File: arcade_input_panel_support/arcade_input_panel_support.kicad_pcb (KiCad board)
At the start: 2 copper layers, 116.3 x 103.8 mm, 14 parts, among them J1 Conn_01x15, J10 Conn_01x02, J11 Conn_01x02, J12 Conn_01x02, J13 Conn_01x02, J14 Conn_01x02, J2 Conn_01x14, J3 Conn_01x15, J4 Conn_01x15, J5 Conn_01x05, J6 Conn_01x02, J7 Conn_01x02, J8 Conn_01x02, J9 Conn_01x02

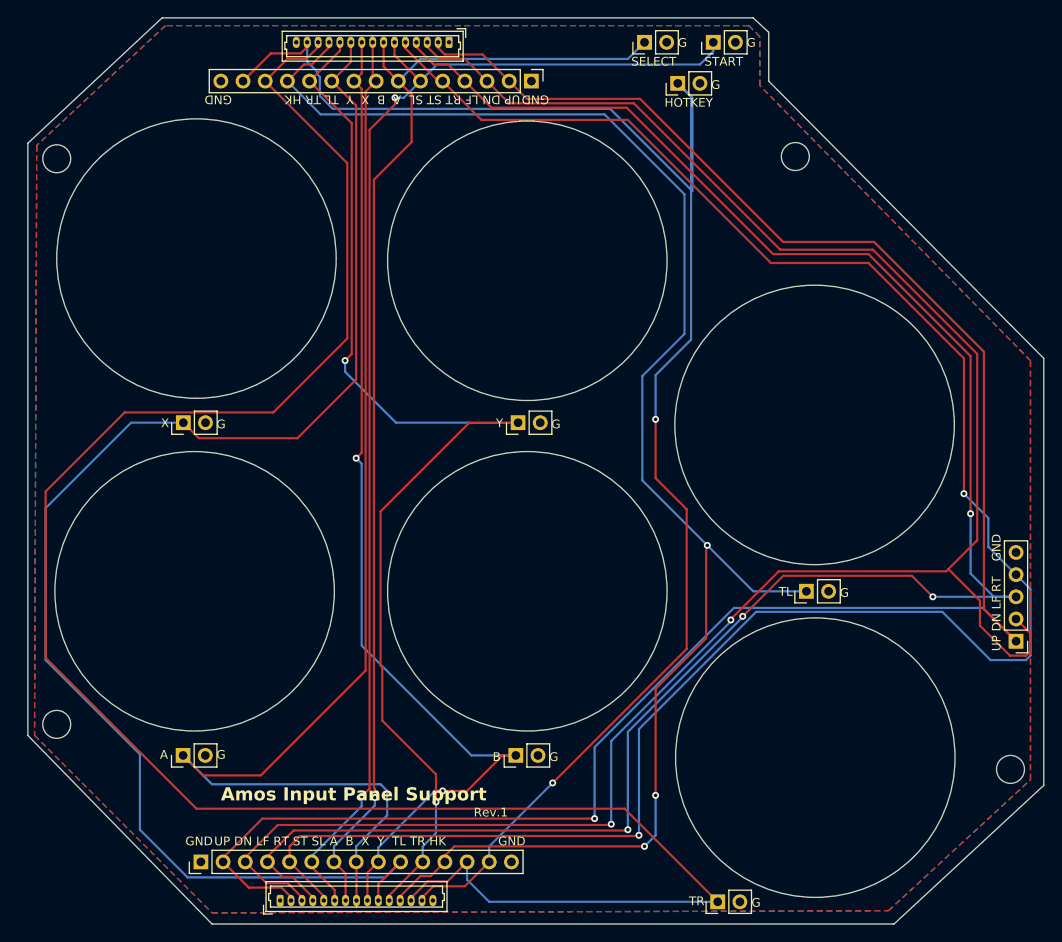
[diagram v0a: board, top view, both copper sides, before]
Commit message: 배선 최적화 및 레이아웃 변경
Signed-off-by: Ju, Gyeong-min <jcmh74@gmail.com>
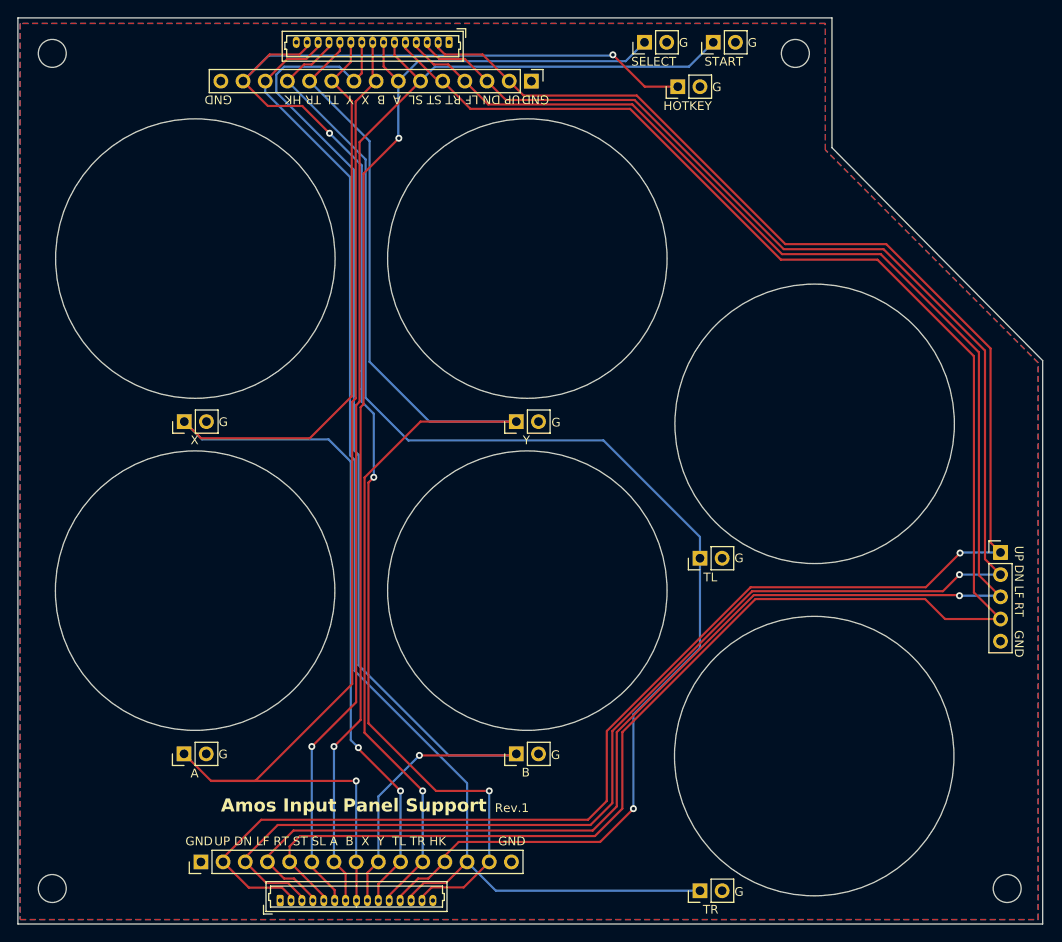
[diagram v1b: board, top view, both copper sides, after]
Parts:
- moved J12 12.8 mm to (114.0, 92.0)
- moved J5 10.3 mm to (148.5, 91.3), turned to 0 degrees
- moved J13 2.40 mm to (114.0, 130.0)
- moved J14 0.38 mm to (111.5, 38.0)
- moved J11 0.24 mm to (93.0, 76.3)
- moved J8 0.21 mm to (55.0, 114.4)
- moved J9 0.19 mm to (93.0, 114.4)
- moved J10 0.17 mm to (55.0, 76.3)
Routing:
- net /TR: track 231.3 -> 144.0 mm
- net /TL: track 185.7 -> 158.2 mm, vias 3 -> 1
- net /X: track 163.4 -> 139.0 mm, vias 0 -> 2
- net /B: track 119.9 -> 138.8 mm, vias 2 -> 1
- net /DOWN: track 232.8 -> 219.0 mm, vias 2 -> 1
- net /RIGHT: track 230.3 -> 219.2 mm, vias 2 -> 0
- net /UP: track 231.7 -> 220.7 mm
- net /HOTKEY: track 188.7 -> 179.7 mm, vias 2 -> 4
- net /A: track 138.5 -> 130.2 mm, vias 0 -> 1
- net /LEFT: track 224.5 -> 217.9 mm, vias 4 -> 1
- net /SELECT: track 134.3 -> 133.0 mm, vias 1 -> 2
- net /START: track 142.3 -> 141.1 mm, vias 2 -> 1
- net /Y: track 133.1 -> 133.4 mm, vias 2 -> 1
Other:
- board size 116.3 x 103.8 mm -> 117.3 x 103.8 mm

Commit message: 커넥터 추가
Signed-off-by: Ju, Gyeong-min <jcmh74@gmail.com>
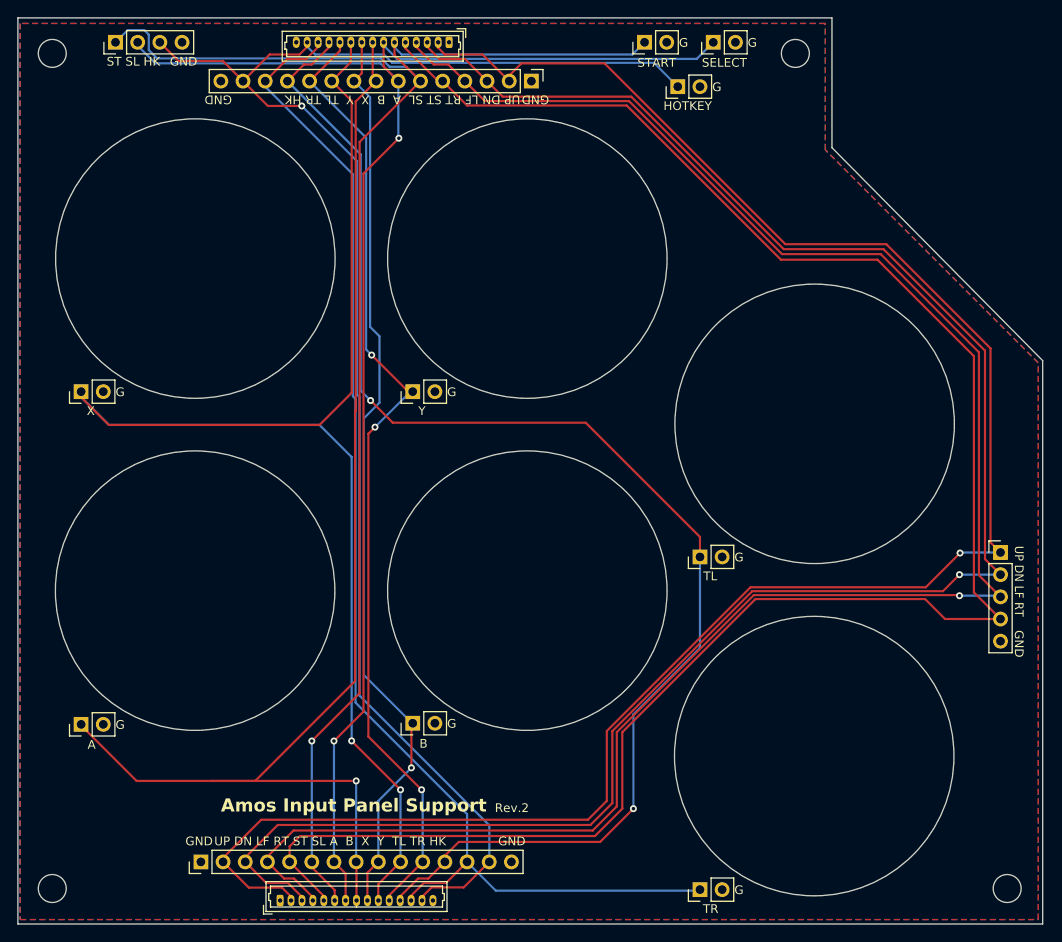
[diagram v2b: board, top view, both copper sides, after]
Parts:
- added J15: Conn_01x04, Connector_PinHeader_2.54mm:PinHeader_1x04_P2.54mm_Vertical, F.Cu at (47.1, 32.9)
- moved J9 12.4 mm to (81.2, 110.9)
- moved J11 12.3 mm to (81.2, 72.9)
- moved J10 12.3 mm to (43.2, 72.9)
- moved J8 12.3 mm to (43.2, 111.0)
- moved J6 7.87 mm to (107.7, 32.9)
- moved J7 7.87 mm to (115.6, 32.9)
- moved J12 0.15 mm to (114.0, 91.8)
- moved J13 0.13 mm to (114.0, 129.9)
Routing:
- net /SELECT: track 133.0 -> 174.1 mm
- net /START: track 141.1 -> 174.8 mm
- net /B: track 138.8 -> 105.1 mm
- net /X: track 139.0 -> 165.1 mm
- net /Y: track 133.4 -> 111.3 mm, vias 1 -> 3
- net /A: track 130.2 -> 143.5 mm
- net /UP: track 220.7 -> 222.7 mm
- net /HOTKEY: track 179.7 -> 179.2 mm, vias 4 -> 1
- net /TL: track 158.2 -> 158.1 mm, vias 1 -> 2
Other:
- board text added: "Rev.2"
- board text added: "ST SL HK"
- board text removed: "Rev.1"

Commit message: 입력 패널 버튼 서포터 rev 2
Signed-off-by: Ju, Gyeong-min <jcmh74@gmail.com>
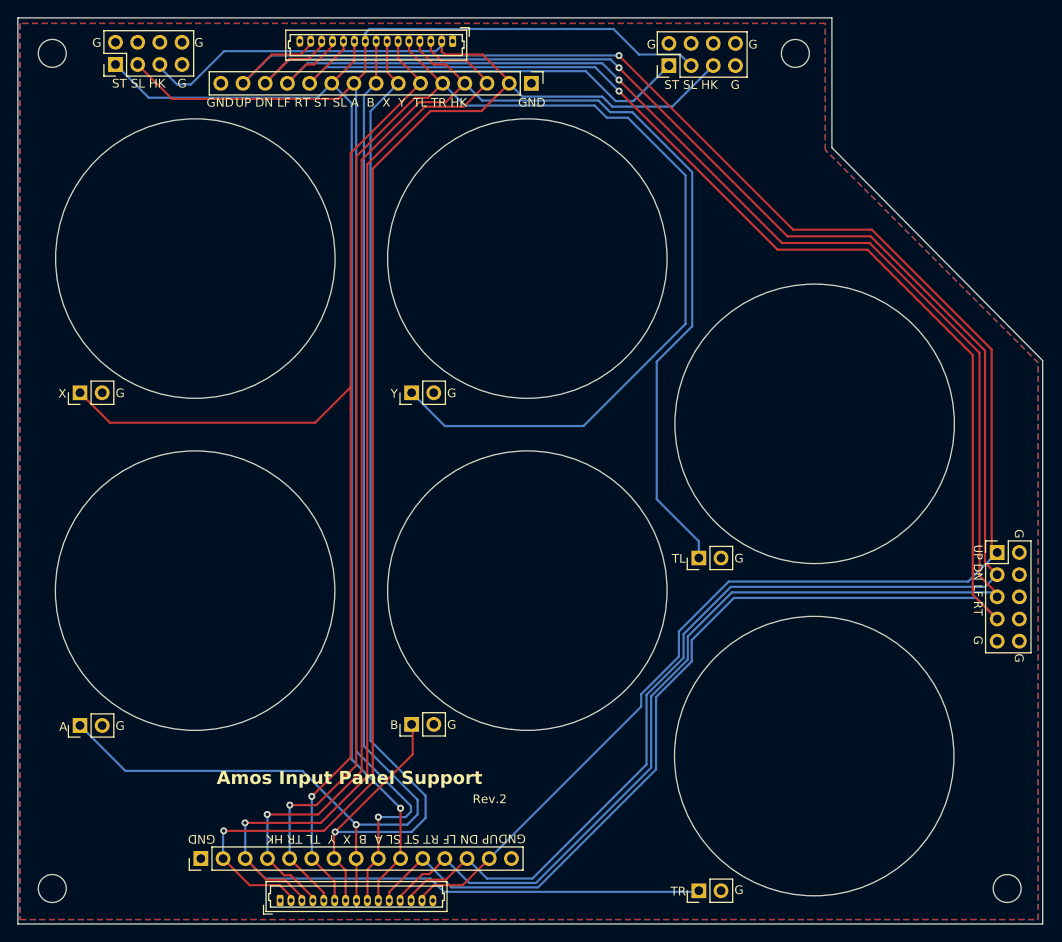
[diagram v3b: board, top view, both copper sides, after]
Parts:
- removed the J14 at (111.5, 38.0)
- removed J6: Conn_01x02, Connector_PinHeader_2.54mm:PinHeader_1x02_P2.54mm_Vertical
- removed the J7 at (115.6, 32.9)
- added J15: Conn_02x04, Connector_PinHeader_2.54mm:PinHeader_2x04_P2.54mm_Vertical, F.Cu at (110.5, 35.6)
- J14: renamed from J15; value Conn_01x04 -> Conn_02x04; footprint Connector_PinHeader_2.54mm:PinHeader_1x04_P2.54mm_Vertical -> Connector_PinHeader_2.54mm:PinHeader_2x04_P2.54mm_Vertical
- J7: renamed from J5; value Conn_01x05 -> Conn_02x05; footprint Connector_PinHeader_2.54mm:PinHeader_1x05_P2.54mm_Vertical -> Connector_PinHeader_2.54mm:PinHeader_2x05_P2.54mm_Vertical
- moved J14 2.54 mm to (47.1, 35.4)
- moved J1 0.43 mm to (85.7, 32.8)
- moved J4 0.38 mm to (56.9, 126.4)
- moved J7 0.38 mm to (148.1, 91.3)
- moved J3 0.25 mm to (94.7, 37.6)
- moved J11 0.18 mm to (81.0, 73.0)
- moved J13 0.18 mm to (113.9, 130.0)
- moved J9 0.18 mm to (81.0, 111.0)
- moved J10 0.18 mm to (43.1, 73.0)
- moved J12 0.18 mm to (113.9, 91.9)
- moved J8 0.18 mm to (43.1, 111.1)
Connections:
- J1 pad 10: /X -> /START
- J1 pad 11: /Y -> /RIGHT
- J1 pad 12: /TL -> /LEFT
- J1 pad 13: /TR -> /DOWN
- J1 pad 14: /HOTKEY -> /UP
- J1 pad 2: /UP -> /HOTKEY
- J1 pad 3: /DOWN -> /TR
- J1 pad 4: /LEFT -> /TL
- J1 pad 5: /RIGHT -> /Y
- J1 pad 6: /START -> /X
- J1 pad 7: /SELECT -> /B
- J1 pad 9: /B -> /SELECT
- J14 pad 2: /SELECT -> GND
- J14 pad 3: /HOTKEY -> /SELECT
- J2 pad 10: /X -> /START
- J2 pad 11: /Y -> /RIGHT
- J2 pad 12: /TL -> /LEFT
- J2 pad 13: /TR -> /DOWN
- J2 pad 14: /HOTKEY -> /UP
- J2 pad 2: /UP -> /HOTKEY
- J2 pad 3: /DOWN -> /TR
- J2 pad 4: /LEFT -> /TL
- J2 pad 5: /RIGHT -> /Y
- J2 pad 6: /START -> /X
- J2 pad 7: /SELECT -> /B
- J2 pad 9: /B -> /SELECT
- J3 pad 10: /X -> /START
- J3 pad 11: /Y -> /RIGHT
- J3 pad 12: /TL -> /LEFT
- J3 pad 13: /TR -> /DOWN
- J3 pad 14: /HOTKEY -> /UP
- J3 pad 2: /UP -> /HOTKEY
- J3 pad 3: /DOWN -> /TR
- J3 pad 4: /LEFT -> /TL
- J3 pad 5: /RIGHT -> /Y
- J3 pad 6: /START -> /X
- J3 pad 7: /SELECT -> /B
- J3 pad 9: /B -> /SELECT
- J4 pad 10: /X -> /START
- J4 pad 11: /Y -> /RIGHT
- J4 pad 12: /TL -> /LEFT
- J4 pad 13: /TR -> /DOWN
- J4 pad 14: /HOTKEY -> /UP
- J4 pad 2: /UP -> /HOTKEY
- J4 pad 3: /DOWN -> /TR
- J4 pad 4: /LEFT -> /TL
- J4 pad 5: /RIGHT -> /Y
- J4 pad 6: /START -> /X
- J4 pad 7: /SELECT -> /B
- J4 pad 9: /B -> /SELECT
- J7 pad 2: /DOWN -> GND
- J7 pad 3: /LEFT -> /DOWN
- J7 pad 4: /RIGHT -> GND
- J7 pad 5: GND -> /LEFT
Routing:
- net /Y: track 111.3 -> 199.1 mm, vias 3 -> 1
- net /TL: track 158.1 -> 196.8 mm, vias 2 -> 1
- net /TR: track 144.0 -> 179.5 mm, vias 0 -> 1
- net /X: track 165.1 -> 139.8 mm, vias 2 -> 1
- net /B: track 105.1 -> 129.4 mm
- net /HOTKEY: track 179.2 -> 195.4 mm
- net /LEFT: track 217.9 -> 222.8 mm
- net /DOWN: track 219.0 -> 223.6 mm
- net /RIGHT: track 219.2 -> 222.7 mm, vias 0 -> 1
- net /UP: track 222.7 -> 220.1 mm
- net /START: track 174.8 -> 173.1 mm
- net /SELECT: track 174.1 -> 172.8 mm, vias 2 -> 1
- net /A: track 143.5 -> 144.2 mm
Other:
- board text removed: "HOTKEY"
- board text removed: "SELECT"
- board text removed: "START"
